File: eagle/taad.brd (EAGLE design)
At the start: 85.8 x 74.3 mm, 56 parts, among them IC1 LD117AS33TR, Q1 16 MHz

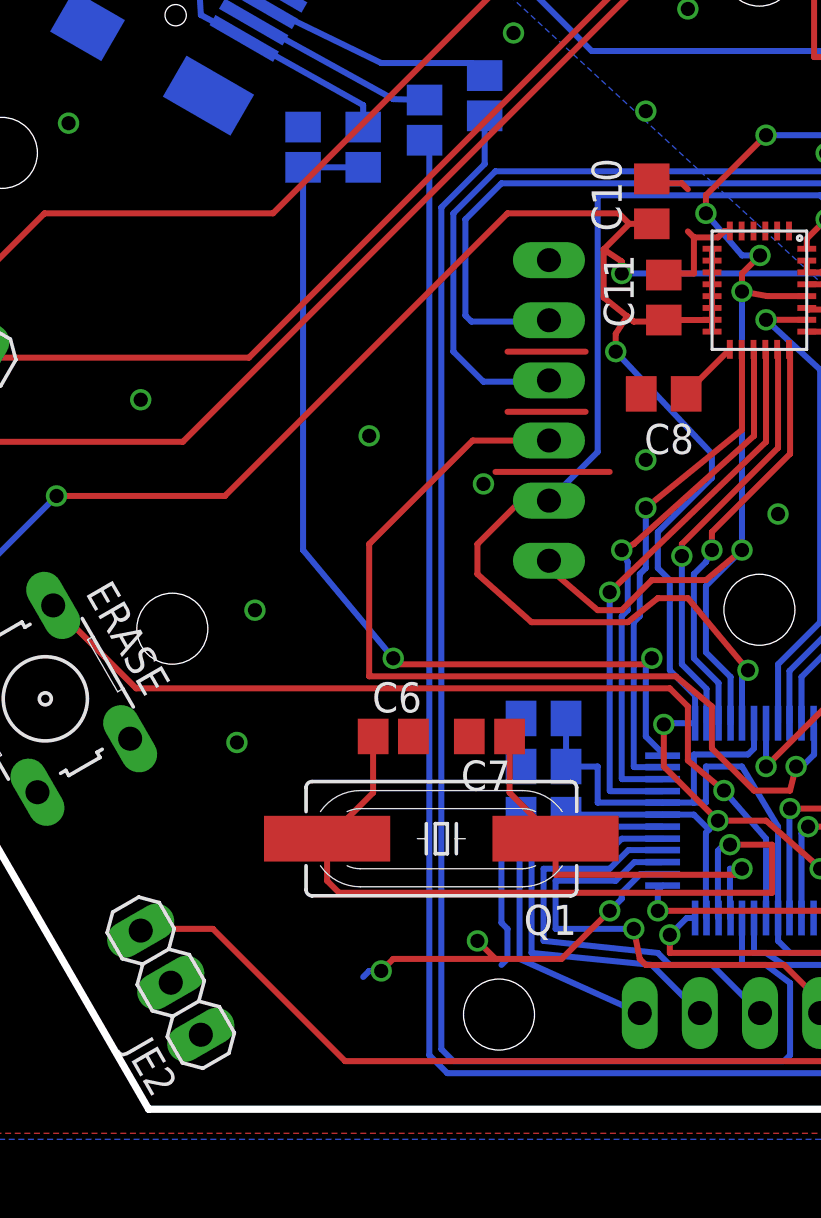
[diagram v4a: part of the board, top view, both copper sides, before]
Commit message: Route USB DDP and DDM around crystal
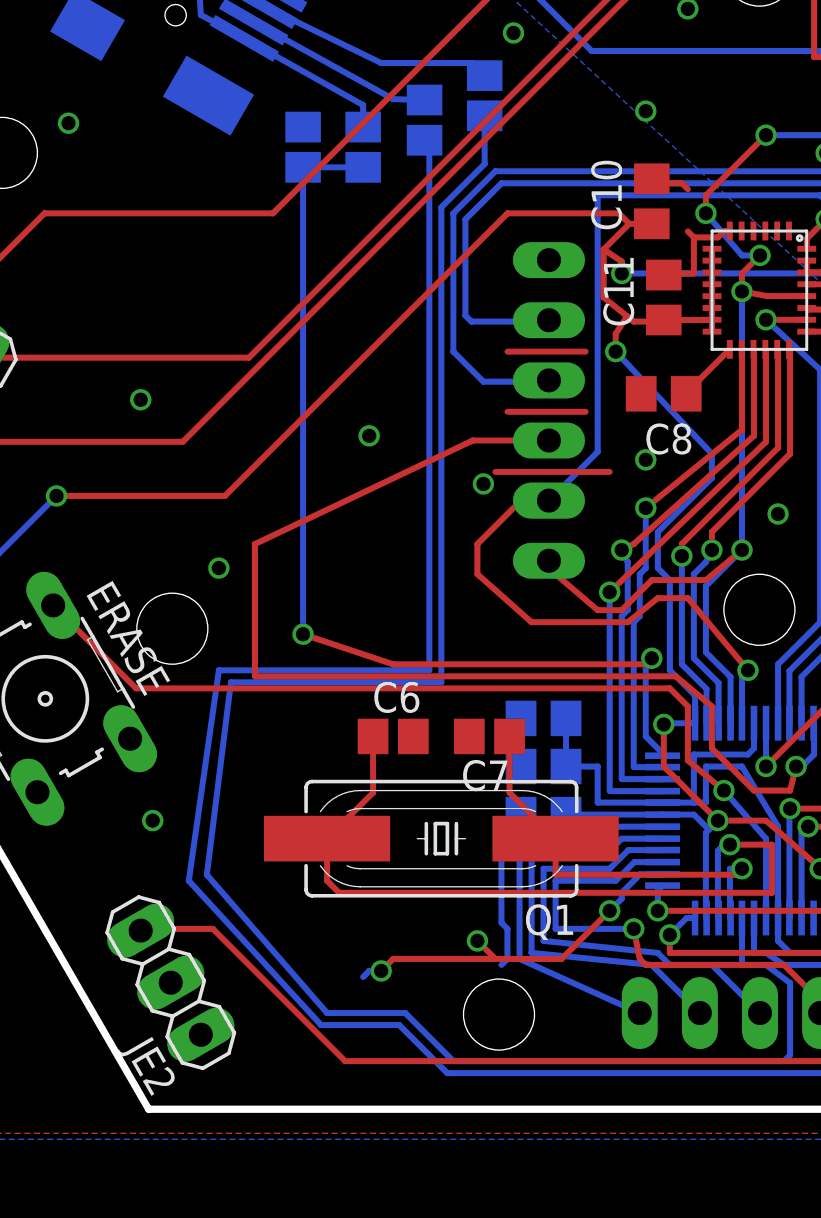
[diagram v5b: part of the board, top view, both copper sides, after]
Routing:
- net DDM: track 66.8 -> 81.8 mm
- net DDP: track 62.5 -> 77.3 mm
- net RF_INT: track 39.1 -> 47.9 mm
- net USB_CONNECTED: track 40.6 -> 42.0 mm
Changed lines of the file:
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@@
 <grid distance="10" unitdist="mil" unit="mil" style="lines" multiple="1" display="yes" altdistance="0.025" altunitdist="inch" altunit="inch"/>
 <layers>
-<layer number="1" name="Top" color="4" fill="1" visible="no" active="yes"/>
+<layer number="1" name="Top" color="4" fill="1" visible="yes" active="yes"/>
 <layer number="16" name="Bottom" color="1" fill="1" visible="yes" active="yes"/>
 <layer number="17" name="Pads" color="2" fill="1" visible="yes" active="yes"/>
@@
 <contactref element="R2" pad="2"/>
 <wire x1="28.754" y1="40.934" x2="28.956" y2="40.732" width="0.254" layer="16"/>
-<wire x1="28.956" y1="40.732" x2="28.956" y2="2.286" width="0.254" layer="16"/>
-<wire x1="28.956" y1="2.286" x2="29.718" y2="1.524" width="0.254" layer="16"/>
+<wire x1="28.956" y1="40.732" x2="28.956" y2="18.542" width="0.254" layer="16"/>
+<wire x1="28.956" y1="18.542" x2="20.066" y2="18.542" width="0.254" layer="16"/>
+<wire x1="20.066" y1="18.542" x2="18.796" y2="9.652" width="0.254" layer="16"/>
+<wire x1="18.796" y1="9.652" x2="24.384" y2="3.556" width="0.254" layer="16"/>
+<wire x1="24.384" y1="3.556" x2="27.686" y2="3.556" width="0.254" layer="16"/>
+<wire x1="27.686" y1="3.556" x2="29.718" y2="1.524" width="0.254" layer="16"/>
 <wire x1="29.718" y1="1.524" x2="46.736" y2="1.524" width="0.254" layer="16"/>
 <wire x1="46.736" y1="1.524" x2="46.482" y2="6.096" width="0.254" layer="16"/>
@@
 <wire x1="32.832" y1="12.446" x2="32.832" y2="12.38" width="0.254" layer="16"/>
 <wire x1="32.832" y1="12.38" x2="33.02" y2="12.192" width="0.254" layer="16"/>
-<via x="20.828" y="15.494" extent="1-16" drill="0.6" diameter="0.254"/>
-<via x="21.59" y="21.082" extent="1-16" drill="0.6" diameter="0.254"/>
+<via x="17.272" y="12.192" extent="1-16" drill="0.6" diameter="0.254"/>
+<via x="20.066" y="22.86" extent="1-16" drill="0.6" diameter="0.254"/>
 <wire x1="33.02" y1="12.192" x2="32.766" y2="12.192" width="0.254" layer="16"/>
 <wire x1="32.766" y1="12.192" x2="32.004" y2="11.43" width="0.254" layer="16"/>
@@
 <wire x1="38.354" y1="19.05" x2="38.1" y2="18.796" width="0.254" layer="1"/>
 <wire x1="38.1" y1="18.796" x2="27.432" y2="18.796" width="0.254" layer="1"/>
-<wire x1="27.432" y1="18.796" x2="27.432" y2="19.05" width="0.254" layer="1"/>
-<via x="27.432" y="19.05" extent="1-16" drill="0.6" diameter="0.254"/>
-<wire x1="27.432" y1="19.05" x2="23.622" y2="23.622" width="0.254" layer="16"/>
-<wire x1="23.622" y1="23.622" x2="23.622" y2="39.79" width="0.254" layer="16"/>
+<wire x1="27.432" y1="18.796" x2="23.622" y2="20.066" width="0.254" layer="1"/>
+<via x="23.622" y="20.066" extent="1-16" drill="0.6" diameter="0.254"/>
+<wire x1="23.622" y1="20.066" x2="23.622" y2="39.79" width="0.254" layer="16"/>
 <wire x1="23.622" y1="39.79" x2="26.162" y2="39.79" width="0.254" layer="16"/>
 </signal>
@@
 <wire x1="40.894" y1="15.24" x2="40.894" y2="17.018" width="0.254" layer="1"/>
 <wire x1="40.894" y1="17.018" x2="39.37" y2="18.288" width="0.254" layer="1"/>
-<wire x1="39.37" y1="18.288" x2="26.416" y2="18.288" width="0.254" layer="1"/>
-<wire x1="26.416" y1="18.288" x2="26.416" y2="23.876" width="0.254" layer="1"/>
-<wire x1="26.416" y1="23.876" x2="30.79" y2="28.25" width="0.254" layer="1"/>
+<wire x1="39.37" y1="18.288" x2="21.59" y2="18.288" width="0.254" layer="1"/>
+<wire x1="21.59" y1="18.288" x2="21.59" y2="23.876" width="0.254" layer="1"/>
+<wire x1="21.59" y1="23.876" x2="30.79" y2="28.25" width="0.254" layer="1"/>
 <wire x1="30.79" y1="28.25" x2="34.01" y2="28.25" width="0.254" layer="1"/>
 </signal>
@@
 <wire x1="44.196" y1="2.286" x2="43.942" y2="2.032" width="0.254" layer="16"/>
 <wire x1="43.942" y1="2.032" x2="29.972" y2="2.032" width="0.254" layer="16"/>
-<wire x1="29.972" y1="2.032" x2="29.464" y2="2.54" width="0.254" layer="16"/>
-<wire x1="29.464" y1="2.54" x2="29.464" y2="38.1" width="0.254" layer="16"/>
+<wire x1="29.972" y1="2.032" x2="27.94" y2="4.064" width="0.254" layer="16"/>
+<wire x1="27.94" y1="4.064" x2="24.638" y2="4.064" width="0.254" layer="16"/>
+<wire x1="24.638" y1="4.064" x2="19.558" y2="9.906" width="0.254" layer="16"/>
+<wire x1="19.558" y1="9.906" x2="20.574" y2="18.034" width="0.254" layer="16"/>
+<wire x1="20.574" y1="18.034" x2="29.464" y2="18.034" width="0.254" layer="16"/>
+<wire x1="29.464" y1="18.034" x2="29.464" y2="38.1" width="0.254" layer="16"/>
 <wire x1="29.464" y1="38.1" x2="31.294" y2="39.93" width="0.254" layer="16"/>
 <wire x1="31.294" y1="39.93" x2="31.294" y2="41.966" width="0.254" layer="16"/>
